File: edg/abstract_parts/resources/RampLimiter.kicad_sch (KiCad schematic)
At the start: 4 parts

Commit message: docs
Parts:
- renumbered cgd to cap_gd, cgs to cap_gs
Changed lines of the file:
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@@
 		(dnp no)
 		(fields_autoplaced yes)
-		(property "Reference" "cgd"
+		(property "Reference" "cap_gd"
 			(at 143.51 92.0749 0)
 			(effects
@@
 			(project ""
 				(path "/b55f6c44-5d5d-4524-bb86-893662f64598"
-					(reference "cgd")
+					(reference "cap_gd")
 					(unit 1)
 				)
@@
 		(dnp no)
 		(fields_autoplaced yes)
-		(property "Reference" "cgs"
+		(property "Reference" "cap_gs"
 			(at 124.46 92.0749 0)
 			(effects
@@
 			(project "RampLimiter"
 				(path "/b55f6c44-5d5d-4524-bb86-893662f64598"
-					(reference "cgs")
+					(reference "cap_gs")
 					(unit 1)
 				)

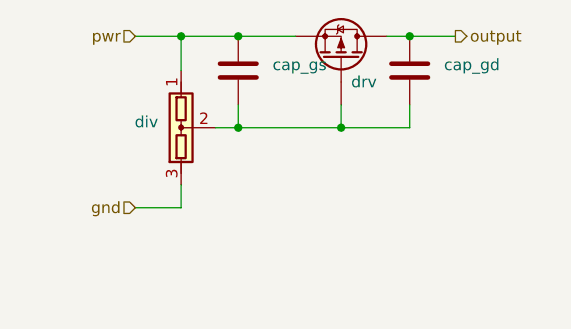
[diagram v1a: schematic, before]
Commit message: wip gate threshold spec and top level test
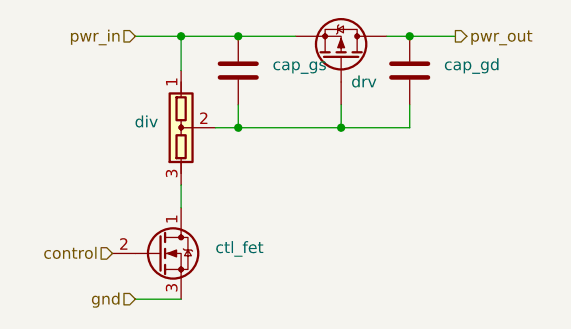
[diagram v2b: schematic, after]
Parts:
- added ctl_fet: ~, symbol Device:Q_NMOS_DGS
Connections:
- net gnd: now also ctl_fet.3 (S); no longer div.3
- net output renamed pwr_out
- net pwr renamed pwr_in
- new net: ctl_fet.1 (D), div.3
- new net control: ctl_fet.2 (G)
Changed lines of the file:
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@@
+	(wire
+		(pts
+			(xy 109.22 118.11) (xy 114.3 118.11)
+		)
+		(stroke
+			(width 0)
+			(type default)
+		)
+	)
 	(wire
 		(pts
@@
 	(wire
 		(pts
-			(xy 109.22 107.95) (xy 114.3 107.95)
-		)
-		(stroke
-			(width 0)
-			(type default)
-		)
-	)
-	(wire
-		(pts
 			(xy 120.65 99.06) (xy 132.08 99.06)
 		)
@@
 		)
 	)
-	(hierarchical_label "pwr"
+	(hierarchical_label "pwr_in"
 		(shape input)
 		(at 109.22 88.9 180)
@@
 		)
 	)
-	(hierarchical_label "output"
+	(hierarchical_label "pwr_out"
 		(shape output)
 		(at 144.78 88.9 0)
@@
 		)
 	)
+	(hierarchical_label "control"
+		(shape input)
+		(at 106.68 113.03 180)
+		(fields_autoplaced yes)
+		(effects
+			(font
+				(size 1.27 1.27)
+			)
+			(justify right)
+		)
+	)
 	(hierarchical_label "gnd"
 		(shape input)
-		(at 109.22 107.95 180)
+		(at 109.22 118.11 180)
 		(fields_autoplaced yes)
 		(effects
@@
 		)
 	)
+	(symbol
+		(lib_id "Device:Q_NMOS_DGS")
+		(at 111.76 113.03 0)
+		(unit 1)
+		(exclude_from_sim no)
+		(in_bom yes)
+		(on_board yes)
+		(dnp no)
+		(fields_autoplaced yes)
+		(property "Reference" "ctl_fet"
+			(at 118.11 112.3949 0)
+			(effects
+				(font
+					(size 1.27 1.27)
+				)
+				(justify left)
+			)
+		)
+		(property "Value" "~"
+			(at 118.11 114.3 0)
+			(effects
+				(font
+					(size 1.27 1.27)
+				)
+				(justify left)
+			)
+		)
+		(property "Footprint" ""
+			(at 116.84 110.49 0)
+			(effects
+				(font
+					(size 1.27 1.27)
+				)
+				(hide yes)
+			)
+		)
+		(property "Datasheet" "~"
+			(at 111.76 113.03 0)
+			(effects
+				(font
+					(size 1.27 1.27)
+				)
+				(hide yes)
+			)
+		)
+		(property "Description" "N-MOSFET transistor, drain/gate/source"
+			(at 111.76 113.03 0)
+			(effects
+				(font
+					(size 1.27 1.27)
+				)
+				(hide yes)
+			)
+		)
+		(pin "1"
+		)
+		(pin "2"
+		)
+		(pin "3"
+		)
+		(instances
+			(project ""
+				(path "/b55f6c44-5d5d-4524-bb86-893662f64598"
+					(reference "ctl_fet")
+					(unit 1)
+				)
+			)
+		)
+	)
